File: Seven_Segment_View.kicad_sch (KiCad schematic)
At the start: 51 parts, among them U1 DA56-11SURKWA, U2 4543, U3 4543, U4 4543, U5 DA56-11SURKWA, U6 4543, U7 4543, U8 DA56-11SURKWA, U9 4543

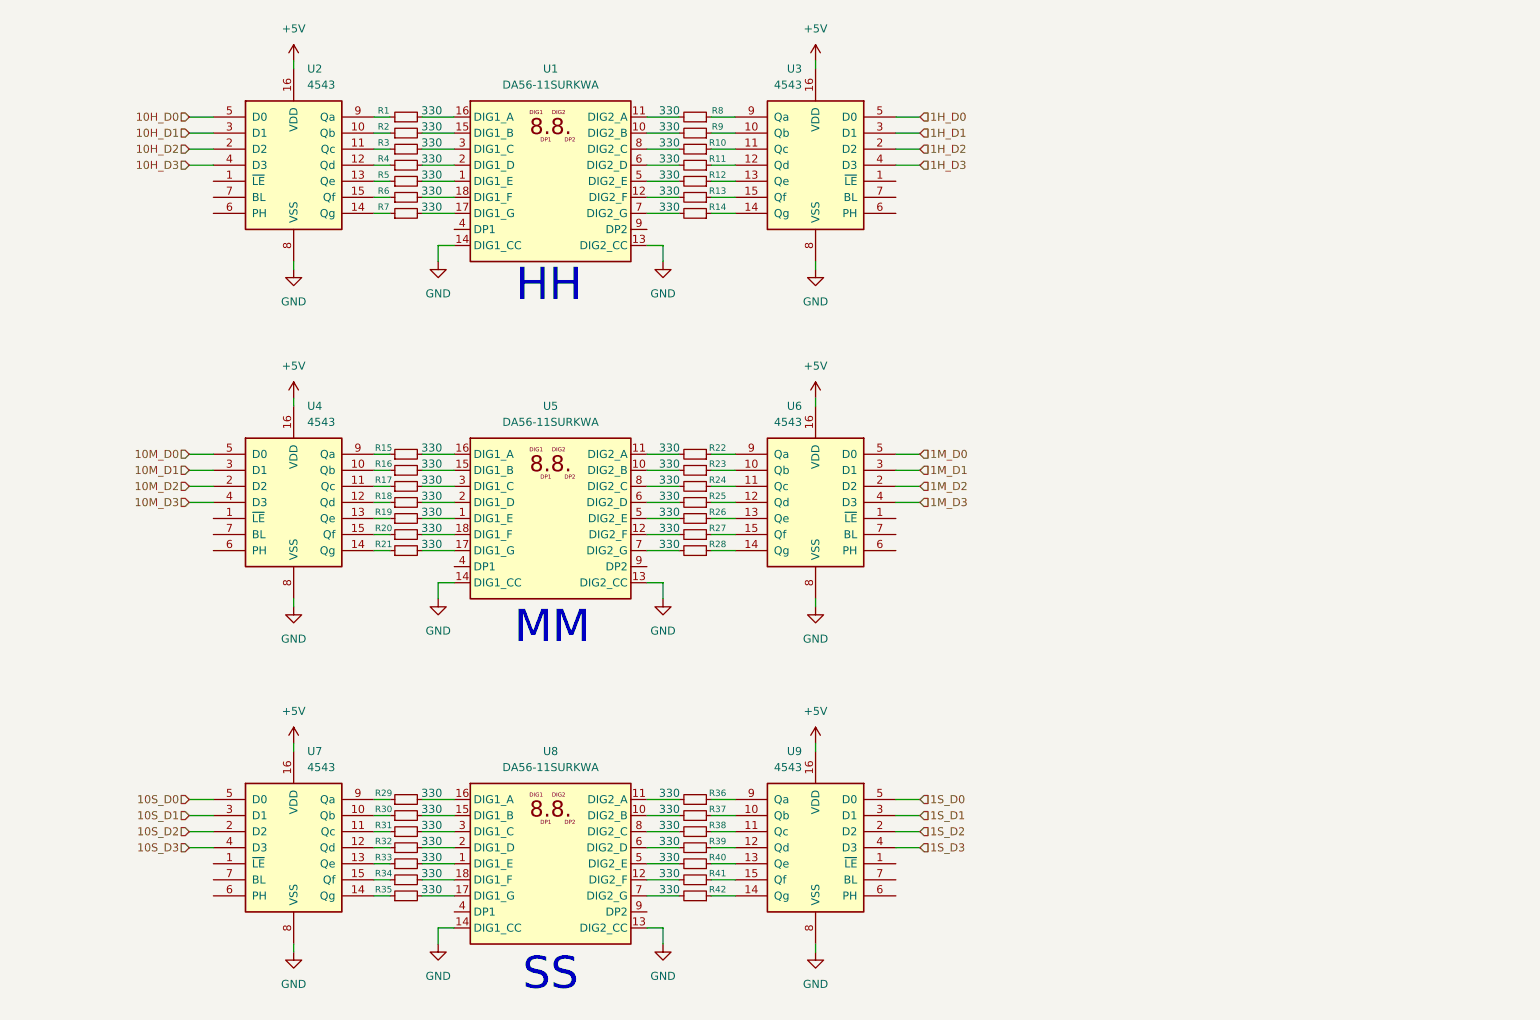
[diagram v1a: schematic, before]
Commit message: Add initial component list for Digital Clock project
- Created a new CSV file 'Digital_Clock_6_Digits.csv' to define components.
- Included details such as designators, footprints, quantities, and designations for resistors, connectors, and ICs.
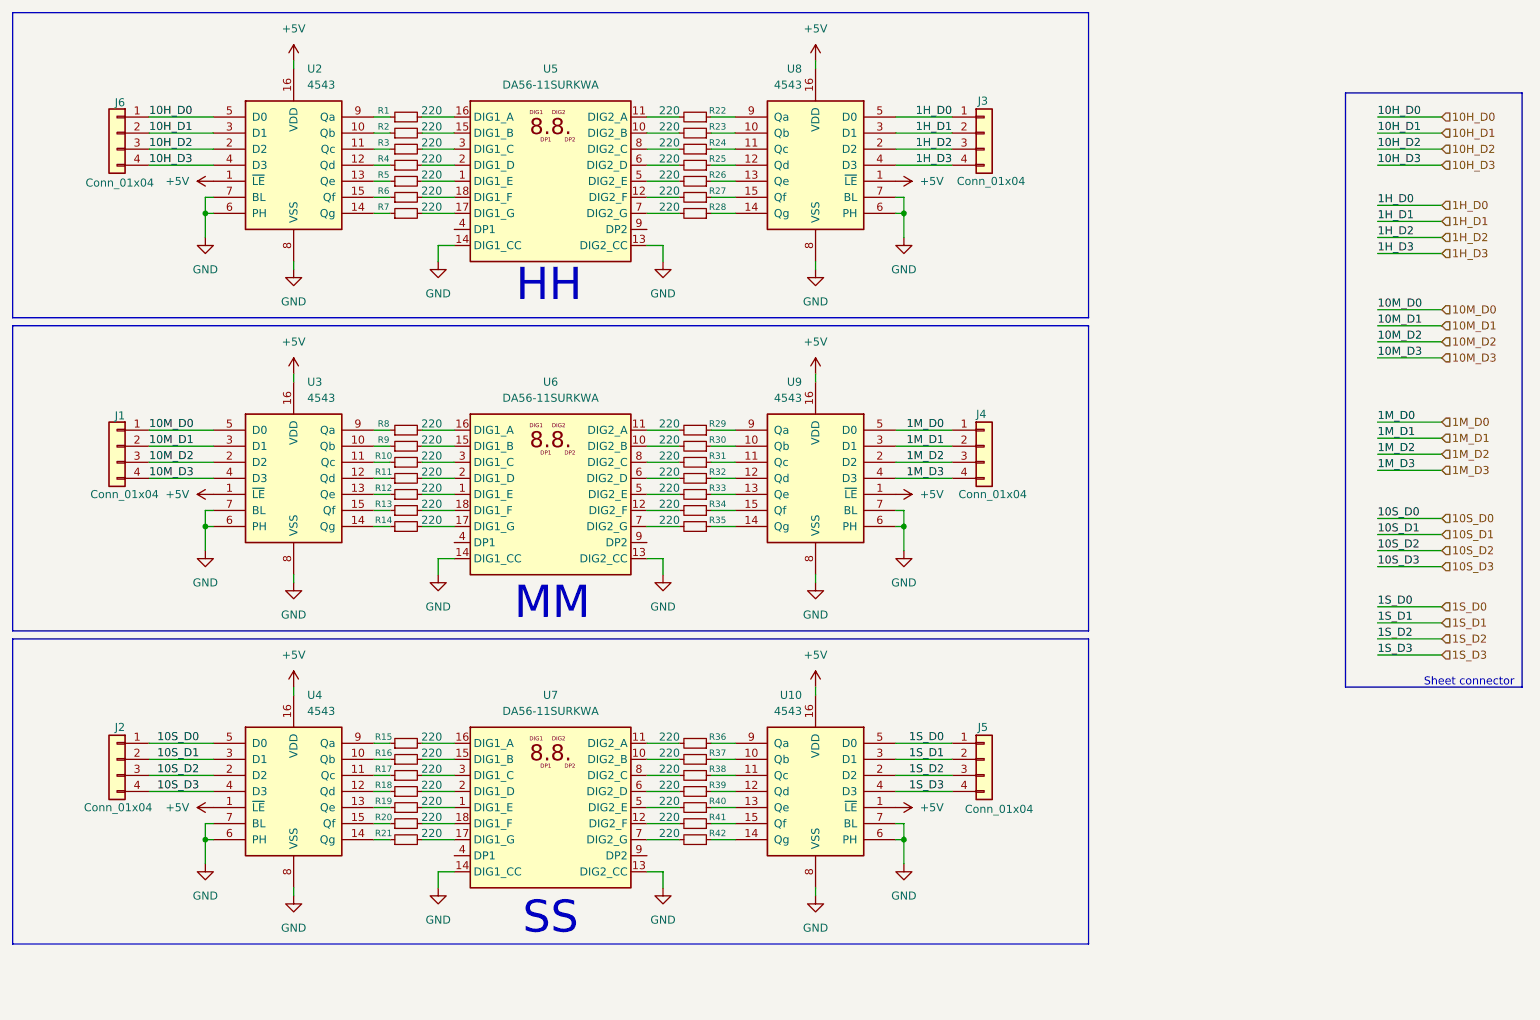
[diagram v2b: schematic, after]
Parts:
- added J1, J2, J3, J4, J5, J6: Conn_01x04, Connector_PinHeader_2.54mm:PinHeader_1x04_P2.54mm_Vertical, symbol Connector_Generic:Conn_01x04
- R1, R2, R3, R36, R37, R38, R39, R4, R40, R41, R42, R5, R6, R7: value 330 -> 220; footprint (none) -> Resistor_SMD:R_0603_1608Metric
- R10: renamed from R17; value 330 -> 220; footprint (none) -> Resistor_SMD:R_0603_1608Metric
- R11: renamed from R18; value 330 -> 220; footprint (none) -> Resistor_SMD:R_0603_1608Metric
- R12: renamed from R19; value 330 -> 220; footprint (none) -> Resistor_SMD:R_0603_1608Metric
- R13: renamed from R20; value 330 -> 220; footprint (none) -> Resistor_SMD:R_0603_1608Metric
- R14: renamed from R21; value 330 -> 220; footprint (none) -> Resistor_SMD:R_0603_1608Metric
- R15: renamed from R29; value 330 -> 220; footprint (none) -> Resistor_SMD:R_0603_1608Metric
- R16: renamed from R30; value 330 -> 220; footprint (none) -> Resistor_SMD:R_0603_1608Metric
- R17: renamed from R31; value 330 -> 220; footprint (none) -> Resistor_SMD:R_0603_1608Metric
- R18: renamed from R32; value 330 -> 220; footprint (none) -> Resistor_SMD:R_0603_1608Metric
- R19: renamed from R33; value 330 -> 220; footprint (none) -> Resistor_SMD:R_0603_1608Metric
- R20: renamed from R34; value 330 -> 220; footprint (none) -> Resistor_SMD:R_0603_1608Metric
- R21: renamed from R35; value 330 -> 220; footprint (none) -> Resistor_SMD:R_0603_1608Metric
- R22: renamed from R8; value 330 -> 220; footprint (none) -> Resistor_SMD:R_0603_1608Metric
- R23: renamed from R9; value 330 -> 220; footprint (none) -> Resistor_SMD:R_0603_1608Metric
- R24: renamed from R10; value 330 -> 220; footprint (none) -> Resistor_SMD:R_0603_1608Metric
- R25: renamed from R11; value 330 -> 220; footprint (none) -> Resistor_SMD:R_0603_1608Metric
- R26: renamed from R12; value 330 -> 220; footprint (none) -> Resistor_SMD:R_0603_1608Metric
- R27: renamed from R13; value 330 -> 220; footprint (none) -> Resistor_SMD:R_0603_1608Metric
- R28: renamed from R14; value 330 -> 220; footprint (none) -> Resistor_SMD:R_0603_1608Metric
- R29: renamed from R22; value 330 -> 220; footprint (none) -> Resistor_SMD:R_0603_1608Metric
- R30: renamed from R23; value 330 -> 220; footprint (none) -> Resistor_SMD:R_0603_1608Metric
- R31: renamed from R24; value 330 -> 220; footprint (none) -> Resistor_SMD:R_0603_1608Metric
- R32: renamed from R25; value 330 -> 220; footprint (none) -> Resistor_SMD:R_0603_1608Metric
- R33: renamed from R26; value 330 -> 220; footprint (none) -> Resistor_SMD:R_0603_1608Metric
- R34: renamed from R27; value 330 -> 220; footprint (none) -> Resistor_SMD:R_0603_1608Metric
- R35: renamed from R28; value 330 -> 220; footprint (none) -> Resistor_SMD:R_0603_1608Metric
- R8: renamed from R15; value 330 -> 220; footprint (none) -> Resistor_SMD:R_0603_1608Metric
- R9: renamed from R16; value 330 -> 220; footprint (none) -> Resistor_SMD:R_0603_1608Metric
- U10: renamed from U9; footprint (none) -> Package_DIP:DIP-16_W7.62mm_Socket_LongPads
- U2: footprint (none) -> Package_DIP:DIP-16_W7.62mm_Socket_LongPads
- U3: renamed from U4; footprint (none) -> Package_DIP:DIP-16_W7.62mm_Socket_LongPads
- U4: renamed from U7; footprint (none) -> Package_DIP:DIP-16_W7.62mm_Socket_LongPads
- U8: renamed from U3; footprint (none) -> Package_DIP:DIP-16_W7.62mm_Socket_LongPads
- U9: renamed from U6; footprint (none) -> Package_DIP:DIP-16_W7.62mm_Socket_LongPads
- renumbered U1 to U5, U5 to U6, U8 to U7
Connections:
- net +5V: now also U10.1 (~{LE}), U2.1 (~{LE}), U3.1 (~{LE}), U4.1 (~{LE}), U8.1 (~{LE}), U9.1 (~{LE})
- net 10H_D0: now also J6.1 (Pin_1)
- net 10H_D1: now also J6.2 (Pin_2)
- net 10H_D2: now also J6.3 (Pin_3)
- net 10H_D3: now also J6.4 (Pin_4)
- net 10M_D0: now also J1.1 (Pin_1)
- net 10M_D1: now also J1.2 (Pin_2)
- net 10M_D2: now also J1.3 (Pin_3)
- net 10M_D3: now also J1.4 (Pin_4)
- net 10S_D0: now also J2.1 (Pin_1)
- net 10S_D1: now also J2.2 (Pin_2)
- net 10S_D2: now also J2.3 (Pin_3)
- net 10S_D3: now also J2.4 (Pin_4)
- net 1H_D0: now also J3.1 (Pin_1)
- net 1H_D1: now also J3.2 (Pin_2)
- net 1H_D2: now also J3.3 (Pin_3)
- net 1H_D3: now also J3.4 (Pin_4)
- net 1M_D0: now also J4.1 (Pin_1)
- net 1M_D1: now also J4.2 (Pin_2)
- net 1M_D2: now also J4.3 (Pin_3)
- net 1M_D3: now also J4.4 (Pin_4)
- net 1S_D0: now also J5.1 (Pin_1)
- net 1S_D1: now also J5.2 (Pin_2)
- net 1S_D2: now also J5.3 (Pin_3)
- net 1S_D3: now also J5.4 (Pin_4)
- net GND: now also U10.6 (PH), U10.7 (BL), U2.6 (PH), U2.7 (BL), U3.6 (PH), U3.7 (BL), U4.6 (PH), U4.7 (BL), U8.6 (PH), U8.7 (BL), U9.6 (PH), U9.7 (BL)
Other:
- note added: "Sheet connector"
- moved on the sheet: R10, R11, R12, R13, R14, R15, R16, R17, R18, R19, R20, R21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

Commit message: uodate
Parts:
- added C1, C2, C3, C4, C5, C6: 0.1uF 50V, symbol Device:C_Small
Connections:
- net +5V: now also C1.2, C2.2, C3.2, C4.2, C5.2, C6.2
- net GND: now also C1.1, C2.1, C3.1, C4.1, C5.1, C6.1
